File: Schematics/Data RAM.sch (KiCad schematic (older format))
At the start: 8 parts, among them U10 IDT71256SA12TPG, U11 IDT71256SA12TPG, U8 74LS32, U9 74LS04

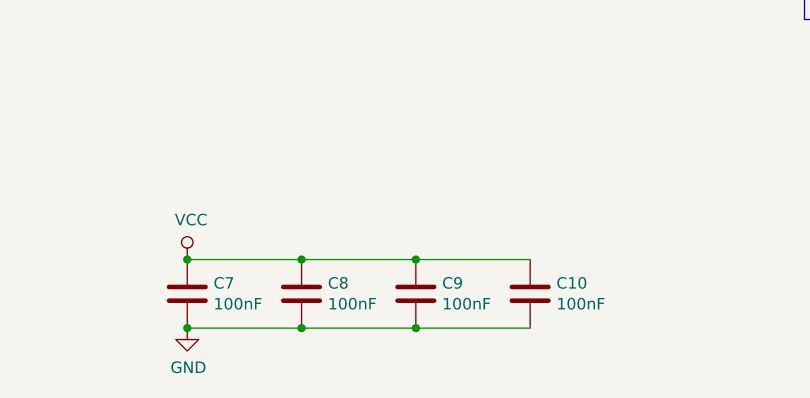
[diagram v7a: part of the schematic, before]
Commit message: Pack parts neatly into a smaller board size.
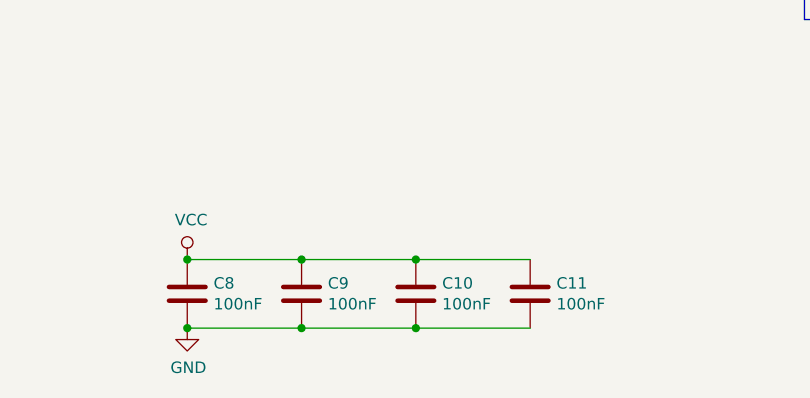
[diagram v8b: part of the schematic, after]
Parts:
- renumbered C9 to C10, C10 to C11, C7 to C8, C8 to C9
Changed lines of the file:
@@
 $EndComp
 $Comp
-L power:GND #PWR019
+L power:GND #PWR021
 U 1 1 5E1EE0BF
 P 6850 3650
-F 0 "#PWR019" H 6850 3400 50  0001 C CNN
+F 0 "#PWR021" H 6850 3400 50  0001 C CNN
 F 1 "GND" H 6855 3477 50  0000 C CNN
 F 2 "" H 6850 3650 50  0001 C CNN
@@
 $EndComp
 $Comp
-L power:GND #PWR021
+L power:GND #PWR023
 U 1 1 5E1EE650
 P 6850 5950
-F 0 "#PWR021" H 6850 5700 50  0001 C CNN
+F 0 "#PWR023" H 6850 5700 50  0001 C CNN
 F 1 "GND" H 6855 5777 50  0000 C CNN
 F 2 "" H 6850 5950 50  0001 C CNN
@@
 $EndComp
 $Comp
-L power:VCC #PWR020
+L power:VCC #PWR022
 U 1 1 5E1EEC64
 P 6850 4150
-F 0 "#PWR020" H 6850 4000 50  0001 C CNN
+F 0 "#PWR022" H 6850 4000 50  0001 C CNN
 F 1 "VCC" H 6867 4323 50  0000 C CNN
 F 2 "" H 6850 4150 50  0001 C CNN
@@
 $EndComp
 $Comp
-L power:VCC #PWR018
+L power:VCC #PWR020
 U 1 1 5E1EF332
 P 6850 1850
-F 0 "#PWR018" H 6850 1700 50  0001 C CNN
+F 0 "#PWR020" H 6850 1700 50  0001 C CNN
 F 1 "VCC" H 6867 2023 50  0000 C CNN
 F 2 "" H 6850 1850 50  0001 C CNN
@@
 P 800 7600
 AR Path="/5D2C07CD/5E262247" Ref="C?"  Part="1"
-AR Path="/5D2C1188/5E262247" Ref="C7"  Part="1"
-F 0 "C7" H 915 7646 50  0000 L CNN
+AR Path="/5D2C1188/5E262247" Ref="C8"  Part="1"
+F 0 "C8" H 915 7646 50  0000 L CNN
 F 1 "100nF" H 915 7555 50  0000 L CNN
 F 2 "Capacitor_THT:C_Disc_D4.3mm_W1.9mm_P5.00mm" H 838 7450 50  0001 C CNN
@@
 P 1300 7600
 AR Path="/5D2C07CD/5E26224D" Ref="C?"  Part="1"
-AR Path="/5D2C1188/5E26224D" Ref="C8"  Part="1"
-F 0 "C8" H 1415 7646 50  0000 L CNN
+AR Path="/5D2C1188/5E26224D" Ref="C9"  Part="1"
+F 0 "C9" H 1415 7646 50  0000 L CNN
 F 1 "100nF" H 1415 7555 50  0000 L CNN
 F 2 "Capacitor_THT:C_Disc_D4.3mm_W1.9mm_P5.00mm" H 1338 7450 50  0001 C CNN
@@
 P 1800 7600
 AR Path="/5D2C07CD/5E262253" Ref="C?"  Part="1"
-AR Path="/5D2C1188/5E262253" Ref="C9"  Part="1"
-F 0 "C9" H 1915 7646 50  0000 L CNN
+AR Path="/5D2C1188/5E262253" Ref="C10"  Part="1"
+F 0 "C10" H 1915 7646 50  0000 L CNN
 F 1 "100nF" H 1915 7555 50  0000 L CNN
 F 2 "Capacitor_THT:C_Disc_D4.3mm_W1.9mm_P5.00mm" H 1838 7450 50  0001 C CNN
@@
 P 2300 7600
 AR Path="/5D2C07CD/5E262259" Ref="C?"  Part="1"
-AR Path="/5D2C1188/5E262259" Ref="C10"  Part="1"
-F 0 "C10" H 2415 7646 50  0000 L CNN
+AR Path="/5D2C1188/5E262259" Ref="C11"  Part="1"
+F 0 "C11" H 2415 7646 50  0000 L CNN
 F 1 "100nF" H 2415 7555 50  0000 L CNN
 F 2 "Capacitor_THT:C_Disc_D4.3mm_W1.9mm_P5.00mm" H 2338 7450 50  0001 C CNN
@@
 P 800 7750
 AR Path="/5D2C07CD/5E26225F" Ref="#PWR?"  Part="1"
-AR Path="/5D2C1188/5E26225F" Ref="#PWR017"  Part="1"
-F 0 "#PWR017" H 800 7500 50  0001 C CNN
+AR Path="/5D2C1188/5E26225F" Ref="#PWR019"  Part="1"
+F 0 "#PWR019" H 800 7500 50  0001 C CNN
 F 1 "GND" H 805 7577 50  0000 C CNN
 F 2 "" H 800 7750 50  0001 C CNN
@@
 P 800 7450
 AR Path="/5D2C07CD/5E262265" Ref="#PWR?"  Part="1"
-AR Path="/5D2C1188/5E262265" Ref="#PWR016"  Part="1"
-F 0 "#PWR016" H 800 7300 50  0001 C CNN
+AR Path="/5D2C1188/5E262265" Ref="#PWR018"  Part="1"
+F 0 "#PWR018" H 800 7300 50  0001 C CNN
 F 1 "VCC" H 817 7623 50  0000 C CNN
 F 2 "" H 800 7450 50  0001 C CNN
